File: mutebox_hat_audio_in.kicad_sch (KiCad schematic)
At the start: 26 parts, among them J1 GPIO, U1 CAT24C256, U2 74LVC157, U3 PCM1862DBT, Y3 XO32

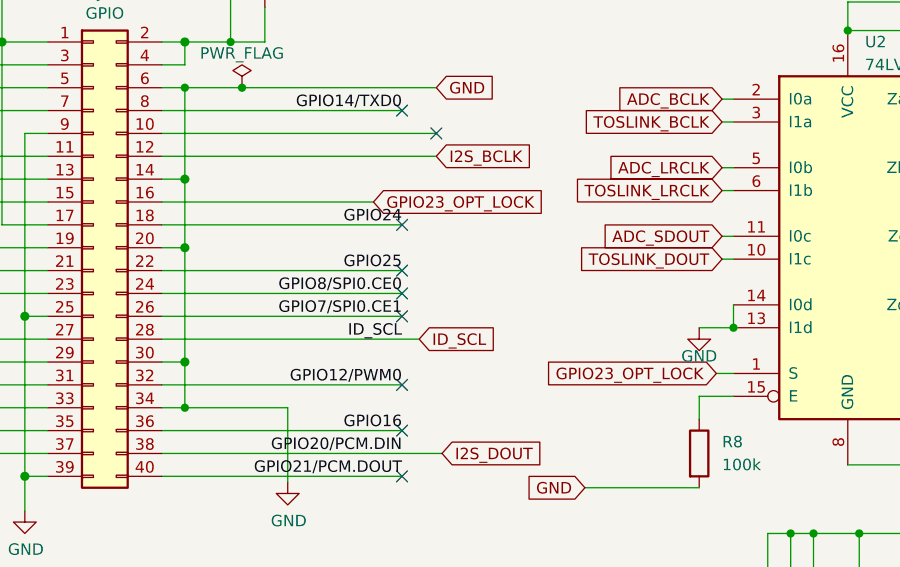
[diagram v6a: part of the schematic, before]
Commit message: Fixed footprint for ADC chip (PCM1862).  Fixed more issues.
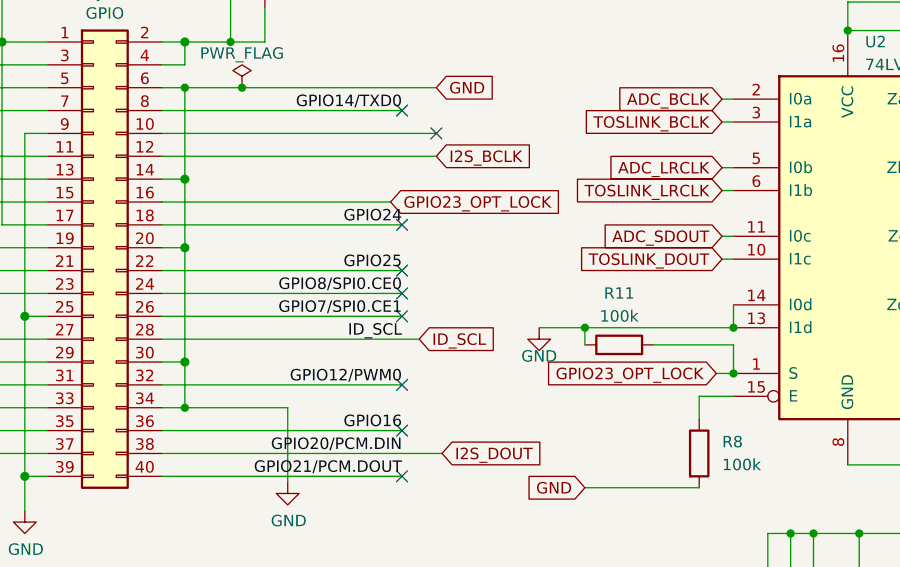
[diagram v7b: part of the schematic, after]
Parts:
- added R11: 100k, symbol Device:R
- U3: footprint Package_SO:TSSOP-32_6.1x11mm_P0.65mm -> Package_SO:TSSOP-30_6.1x9.7mm_P0.65mm
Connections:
- net GND: now also R11.1
- net GPIO23_OPT_LOCK: now also R11.2
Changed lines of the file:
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@@
 	)
 	(junction
+		(at 137.16 64.77)
+		(diameter 0)
+		(color 0 0 0 0)
+	)
+	(junction
 		(at 180.34 23.495)
 		(diameter 0)
@@
 	)
 	(junction
+		(at 120.65 59.69)
+		(diameter 0)
+		(color 0 0 0 0)
+	)
+	(junction
 		(at 71.12 180.34)
 		(diameter 0)
@@
 	(wire
 		(pts
+			(xy 120.65 59.69) (xy 137.16 59.69)
+		)
+		(stroke
+			(width 0)
+			(type default)
+		)
+	)
+	(wire
+		(pts
 			(xy 22.86 27.94) (xy 24.13 27.94)
 		)
@@
 	(wire
 		(pts
+			(xy 137.16 61.595) (xy 137.16 64.77)
+		)
+		(stroke
+			(width 0)
+			(type default)
+		)
+	)
+	(wire
+		(pts
 			(xy 161.29 86.36) (xy 167.64 86.36)
 		)
@@
 	(wire
 		(pts
+			(xy 128.27 61.595) (xy 137.16 61.595)
+		)
+		(stroke
+			(width 0)
+			(type default)
+		)
+	)
+	(wire
+		(pts
 			(xy 73.66 40.64) (xy 104.14 40.64)
 		)
@@
 	(wire
 		(pts
+			(xy 120.65 59.69) (xy 120.65 61.595)
+		)
+		(stroke
+			(width 0)
+			(type default)
+		)
+	)
+	(wire
+		(pts
 			(xy 120.65 149.86) (xy 120.65 156.21)
 		)
@@
 	(wire
 		(pts
-			(xy 133.35 59.69) (xy 137.16 59.69)
+			(xy 115.57 59.69) (xy 120.65 59.69)
 		)
 		(stroke
@@
 	(wire
 		(pts
-			(xy 73.66 45.72) (xy 97.155 45.72)
+			(xy 165.1 121.92) (xy 165.1 130.81)
 		)
 		(stroke
@@
 	(wire
 		(pts
-			(xy 165.1 121.92) (xy 165.1 130.81)
+			(xy 73.66 45.72) (xy 99.06 45.72)
 		)
 		(stroke
@@
 	(global_label "GPIO23_OPT_LOCK"
 		(shape input)
-		(at 97.155 45.72 0)
+		(at 99.06 45.72 0)
 		(fields_autoplaced yes)
 		(effects
@@
 		)
 		(property "Intersheetrefs" "${INTERSHEET_REFS}"
-			(at 117.5315 45.72 0)
+			(at 119.4365 45.72 0)
 			(effects
 				(font
@@
 	(symbol
 		(lib_id "power:GND")
-		(at 133.35 59.69 0)
+		(at 115.57 59.69 0)
 		(unit 1)
 		(exclude_from_sim no)
@@
 		(dnp no)
 		(property "Reference" "#PWR07"
-			(at 133.35 66.04 0)
+			(at 115.57 66.04 0)
 			(effects
 				(font
@@
 		)
 		(property "Value" "GND"
-			(at 133.35 62.865 0)
+			(at 115.57 62.865 0)
 			(effects
 				(font
@@
 		)
 		(property "Footprint" ""
-			(at 133.35 59.69 0)
+			(at 115.57 59.69 0)
 			(effects
 				(font
@@
 		)
 		(property "Datasheet" ""
-			(at 133.35 59.69 0)
+			(at 115.57 59.69 0)
 			(effects
 				(font
@@
 		)
 		(property "Description" "Power symbol creates a global label with name \"GND\" , ground"
-			(at 133.35 59.69 0)
+			(at 115.57 59.69 0)
 			(effects
 				(font
@@
 			)
 		)
-		(property "Footprint" "Package_SO:TSSOP-32_6.1x11mm_P0.65mm"
+		(property "Footprint" "Package_SO:TSSOP-30_6.1x9.7mm_P0.65mm"
 			(at 151.384 151.384 0)
 			(effects
@@
 					(unit 1)
 				)
+			)
+		)
+	)
+	(symbol
+		(lib_id "Device:R")
+		(at 124.46 61.595 90)
+		(unit 1)
+		(exclude_from_sim no)
+		(in_bom yes)
+		(on_board yes)
+		(dnp no)
+		(fields_autoplaced yes)
+		(property "Reference" "R11"
+			(at 124.46 55.88 90)
+			(effects
+				(font
+					(size 1.27 1.27)
+				)
+			)
+		)
+		(property "Value" "100k"
+			(at 124.46 58.42 90)
+			(effects
+				(font
+					(size 1.27 1.27)
+				)
+			)
+		)
+		(property "Footprint" ""
+			(at 124.46 63.373 90)
+			(effects
+				(font
+					(size 1.27 1.27)
+				)
+				(hide yes)
+			)
+		)
+		(property "Datasheet" "~"
+			(at 124.46 61.595 0)
+			(effects
+				(font
+					(size 1.27 1.27)
+				)
+				(hide yes)
+			)
+		)
+		(property "Description" "Resistor"
+			(at 124.46 61.595 0)
+			(effects
+				(font
+					(size 1.27 1.27)
+				)
+				(hide yes)
+			)
+		)
+		(pin "2"
+		)
+		(pin "1"
+		)
+		(instances
+			(project ""
+				(path "/e63e39d7-6ac0-4ffd-8aa3-1841a4541b55"
+					(reference "R11")
+					(unit 1)
+				)

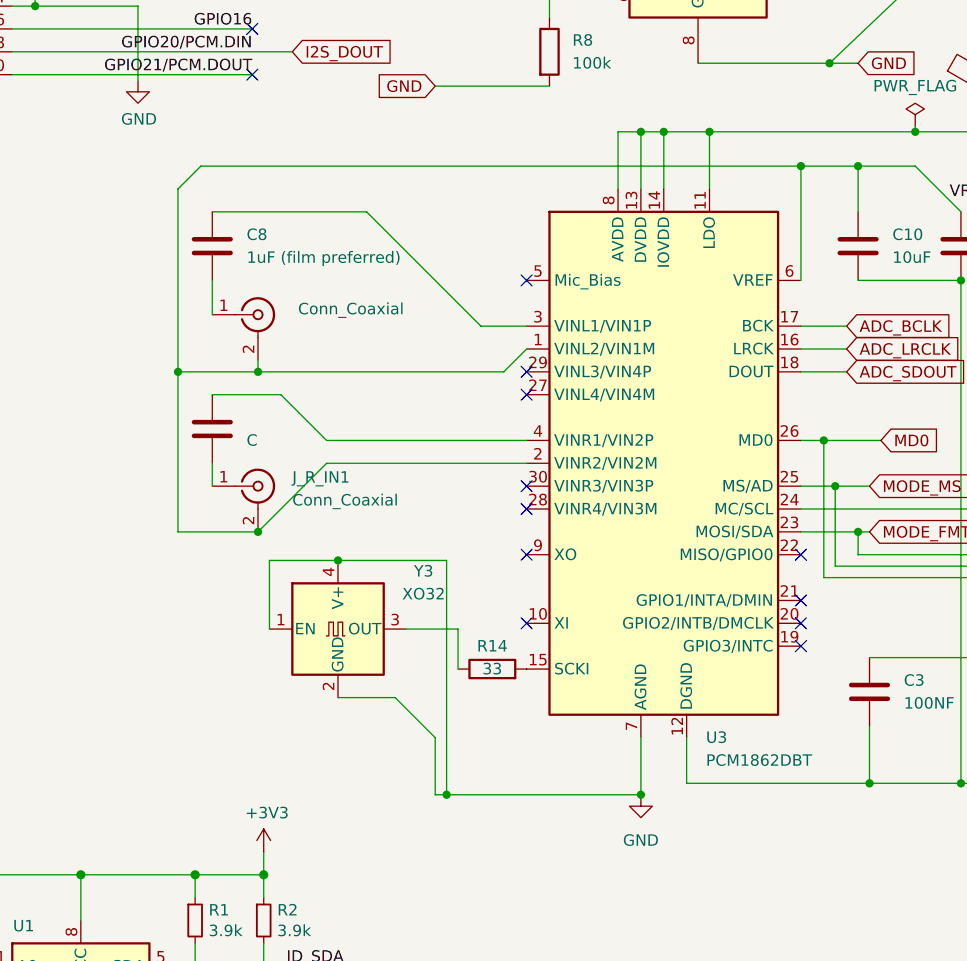
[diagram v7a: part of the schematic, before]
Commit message: Fixed RCA Jack symbols and footprints
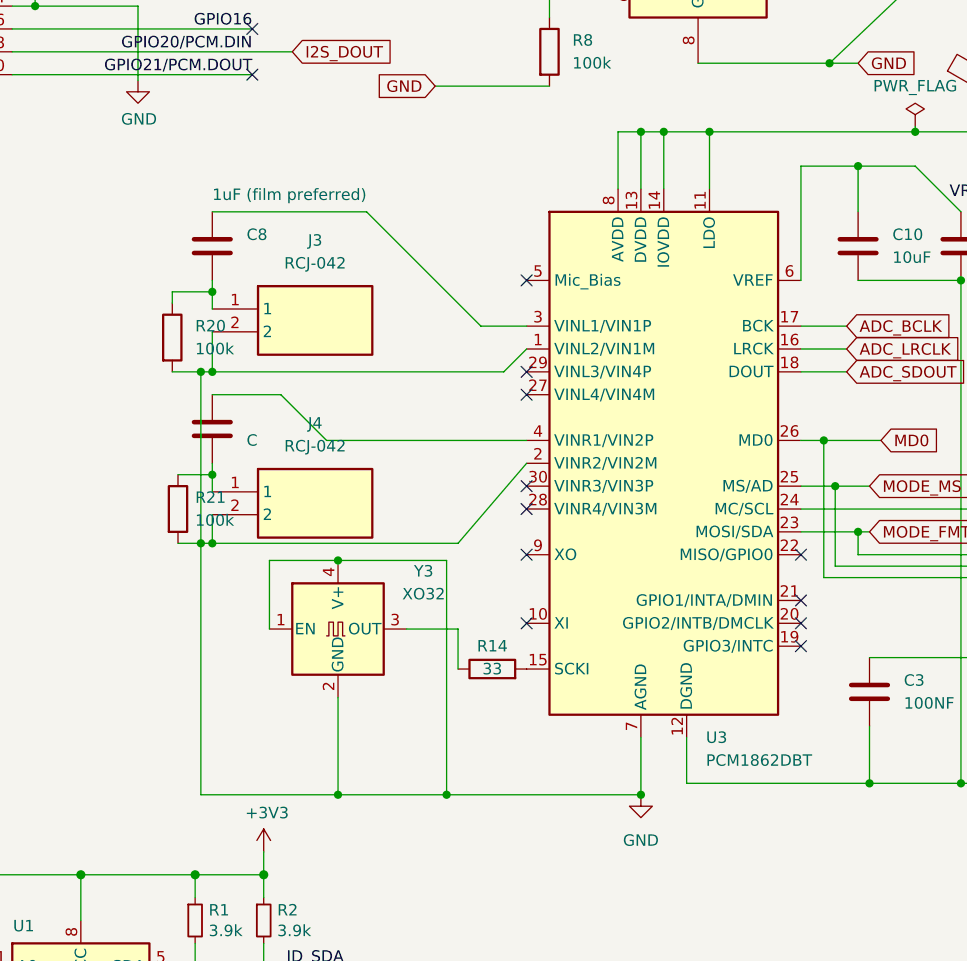
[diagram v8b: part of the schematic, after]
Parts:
- removed J_L_IN1, J_R_IN1: Conn_Coaxial, Connector_Audio:RCJ-043, symbol Connector:Conn_Coaxial
- added J3, J4: RCJ-042, RCJ042, symbol RCJ-042:RCJ-042
- added R20, R21: 100k, Resistor_SMD:R_0805_2012Metric_Pad1.20x1.40mm_HandSolder, symbol Device:R
- R11: footprint (none) -> Resistor_SMD:R_0805_2012Metric_Pad1.20x1.40mm_HandSolder
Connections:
- net GND: now also U3.1 (VINL2/VIN1M), U3.2 (VINR2/VIN2M), J3.2, J4.2, R20.2, R21.2
- net VREF: no longer U3.1 (VINL2/VIN1M), U3.2 (VINR2/VIN2M)
- net at C8.2: now also J3.1, R20.1
- net at C9.2: now also J4.1, R21.1
